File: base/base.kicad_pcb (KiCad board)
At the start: 2 copper layers, 51.2 x 20.5 mm, 12 parts, among them J1 Game Boy, J2 Game Gear, J3 Programming, U1 HC139, U2 PIC10F200-IOT

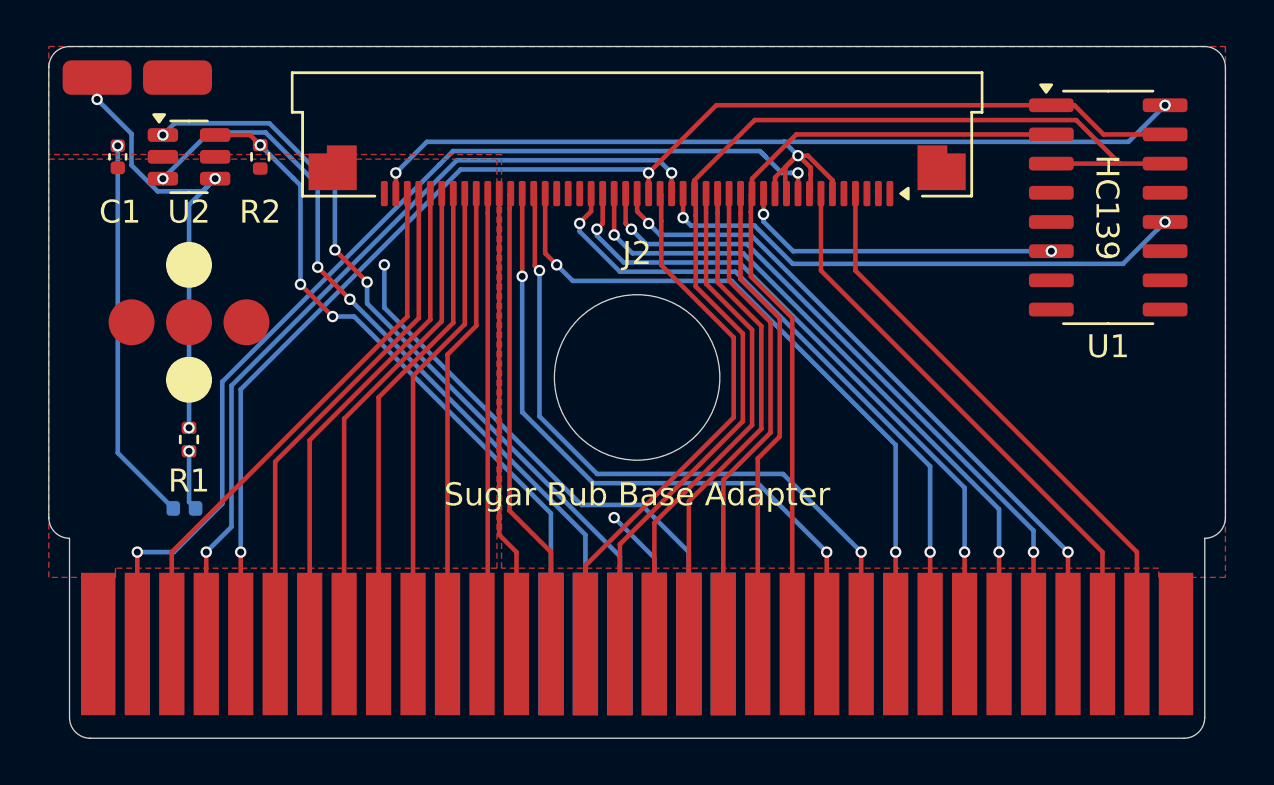
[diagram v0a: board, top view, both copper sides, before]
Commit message: Narrow fingers and move D1 to right side
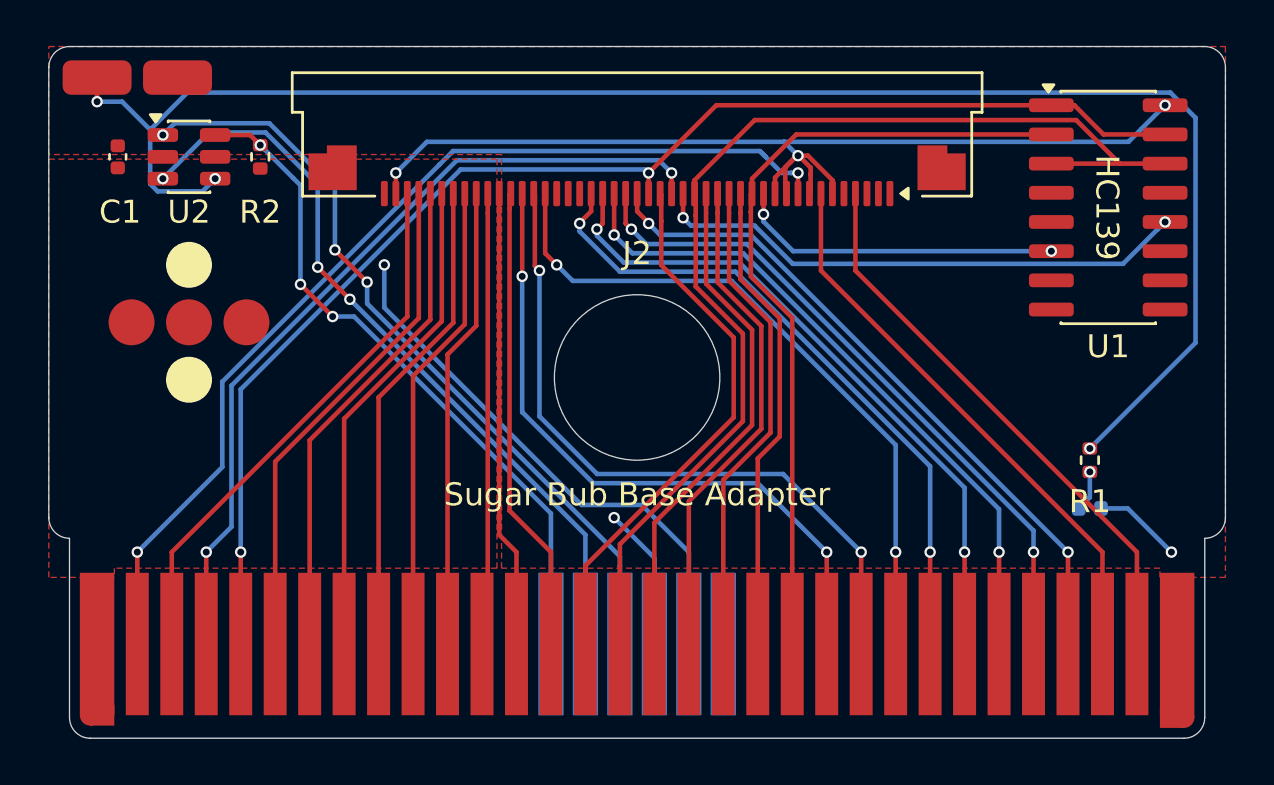
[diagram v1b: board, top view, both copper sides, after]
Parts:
- moved D1 39.4 mm to (119.7, 98.1), turned to 180 degrees
- moved R1 39.2 mm to (119.7, 96.0)
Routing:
- net Net-(U2-GP2): track 19.7 -> 72.3 mm
- net GND: track 23.0 -> 10.1 mm
- net CLK: track 44.7 -> 43.7 mm
- net Net-(D1-A): track 2.61 -> 1.79 mm

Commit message: Adjust adapter PCB dimensions
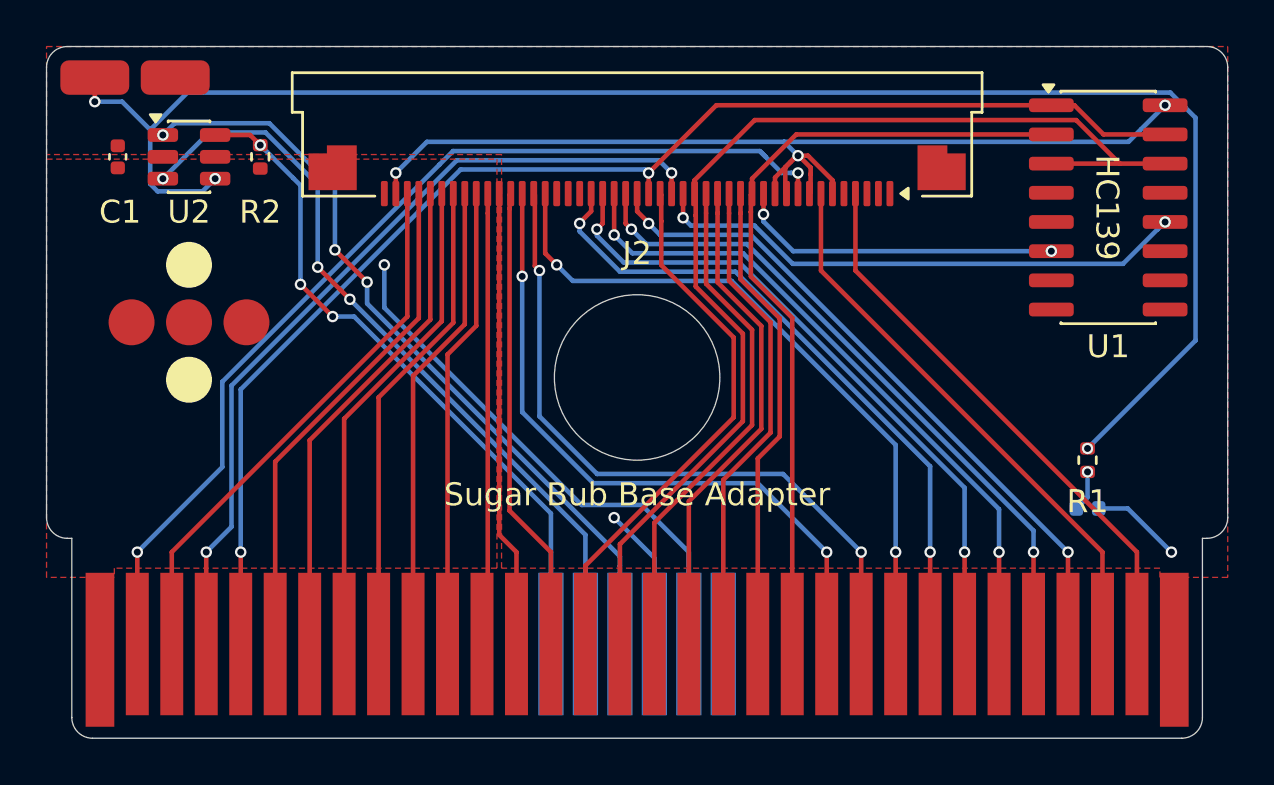
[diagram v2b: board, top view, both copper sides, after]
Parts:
- moved D1 0.10 mm to (119.6, 98.1)
- moved R1 0.10 mm to (119.6, 96.0)
- moved TP1 0.10 mm to (76.4, 79.3)
- moved TP2 0.10 mm to (79.9, 79.3)
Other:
- board size 51.2 x 20.5 mm -> 51.4 x 20.5 mm
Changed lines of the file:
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@@
 	(footprint "Connector_Wire:SolderWirePad_1x01_SMD_1.5x3mm"
 		(layer "F.Cu")
-		(at 80 79.35 90)
+		(at 79.9 79.35 90)
 		(descr "Wire Pad, Square, SMD Pad,  1.5mm x 3mm")
 		(tags "MeasurementPoint Square SMDPad 1.5mmx3mm ")
@@
 	(footprint "Connector_Wire:SolderWirePad_1x01_SMD_1.5x3mm"
 		(layer "F.Cu")
-		(at 76.5 79.35 90)
+		(at 76.4 79.35 90)
 		(descr "Wire Pad, Square, SMD Pad,  1.5mm x 3mm")
 		(tags "MeasurementPoint Square SMDPad 1.5mmx3mm ")
@@
 		(attr smd)
 		(fp_line
-			(start -24.7 3.2)
-			(end -24.7 -4.6)
+			(start -24.6 -4.6)
+			(end -24.8 -4.6)
 			(stroke
 				(width 0.05)
@@
 		)
 		(fp_line
-			(start -23.8 4.1)
-			(end 23.8 4.1)
+			(start -24.6 3.2)
+			(end -24.6 -4.6)
+			(stroke
+				(width 0.05)
+				(type default)
+			)
+			(layer "Edge.Cuts")
+		)
+		(fp_line
+			(start -23.7 4.1)
+			(end 23.7 4.1)
 			(stroke
 				(width 0.05)
@@
 		)
 		(fp_line
-			(start 24.7 3.2)
-			(end 24.7 -4.6)
+			(start 24.6 -4.6)
+			(end 24.8 -4.6)
+			(stroke
+				(width 0.05)
+				(type default)
+			)
+			(layer "Edge.Cuts")
+		)
+		(fp_line
+			(start 24.6 3.2)
+			(end 24.6 -4.6)
 			(stroke
 				(width 0.05)
@@
 		)
 		(fp_arc
-			(start -24.7 -4.6)
-			(mid -25.336396 -4.863604)
-			(end -25.6 -5.5)
+			(start -24.8 -4.6)
+			(mid -25.436396 -4.863604)
+			(end -25.7 -5.5)
 			(stroke
 				(width 0.05)
@@
 		)
 		(fp_arc
-			(start -23.8 4.1)
-			(mid -24.436396 3.836396)
-			(end -24.7 3.2)
+			(start -23.7 4.1)
+			(mid -24.336396 3.836396)
+			(end -24.6 3.2)
 			(stroke
 				(width 0.05)
@@
 		)
 		(fp_arc
-			(start 24.7 3.2)
-			(mid 24.436396 3.836396)
-			(end 23.8 4.1)
+			(start 24.6 3.2)
+			(mid 24.336396 3.836396)
+			(end 23.7 4.1)
 			(stroke
 				(width 0.05)
@@
 		)
 		(fp_arc
-			(start 25.6 -5.5)
-			(mid 25.336396 -4.863604)
-			(end 24.7 -4.6)
+			(start 25.7 -5.5)
+			(mid 25.436396 -4.863604)
+			(end 24.8 -4.6)
 			(stroke
 				(width 0.05)
@@
 			(layer "F.CrtYd")
 		)
-		(pad "1" connect circle
-			(at -23.8 3.1)
-			(size 0.9 0.9)
-			(layers "F.Cu" "F.Mask")
-			(net 26 "+5V")
-			(pinfunction "Pin_1")
-			(pintype "passive")
-		)
-		(pad "1" connect rect
-			(at -23.5 0)
-			(size 1.5 6.2)
-			(layers "F.Cu" "F.Mask")
-			(net 26 "+5V")
-			(pinfunction "Pin_1")
-			(pintype "passive")
-		)
 		(pad "1" connect rect
-			(at -23.275 3.1)
-			(size 1.05 0.9)
+			(at -23.375 0.25)
+			(size 1.25 6.7)
 			(layers "F.Cu" "F.Mask")
 			(net 26 "+5V")
@@
 		)
 		(pad "32" connect rect
-			(at 23.275 3.2)
-			(size 1.05 0.9)
-			(layers "F.Cu" "F.Mask")
-			(net 24 "GND")
-			(pinfunction "Pin_32")
-			(pintype "passive")
-		)
-		(pad "32" connect rect
-			(at 23.5 0.05)
-			(size 1.5 6.3)
-			(layers "F.Cu" "F.Mask")
-			(net 24 "GND")
-			(pinfunction "Pin_32")
-			(pintype "passive")
-		)
-		(pad "32" connect circle
-			(at 23.8 3.2)
-			(size 0.9 0.9)
+			(at 23.375 0.25)
+			(size 1.25 6.7)
 			(layers "F.Cu" "F.Mask")
 			(net 24 "GND")
@@
 	(footprint "Resistor_SMD:R_0402_1005Metric"
 		(layer "F.Cu")
-		(at 119.7 96 -90)
+		(at 119.6 96 -90)
 		(descr "Resistor SMD 0402 (1005 Metric), square (rectangular) end terminal, IPC-7351 nominal, (Body size source: IPC-SM-782 page 72, https://www.pcb-3d.com/wordpress/wp-content/uploads/ipc-sm-782a_amendment_1_and_2.pdf), generated with kicad-footprint-generator")
 		(tags "resistor")
@@
 		)
 		(property "Value" "Game Gear"
-			(at 0 3.45 180)
+			(at 0 4.5 180)
 			(layer "F.Fab")
 			(effects
@@
 			(layer "F.Fab")
 		)
-		(fp_text user "${REFERENCE}"
-			(at 0 0 180)
-			(layer "F.Fab")
-			(effects
-				(font
-					(size 1 1)
-					(thickness 0.15)
-				)
-			)
-		)
 		(pad "1" smd roundrect
 			(at 11 -2.9)
@@
 	(footprint "LED_SMD:LED_0402_1005Metric"
 		(layer "B.Cu")
-		(at 119.7 98.1 180)
+		(at 119.6 98.1 180)
 		(descr "LED SMD 0402 (1005 Metric), square (rectangular) end terminal, IPC-7351 nominal, (Body size source: http://www.tortai-tech.com/upload/download/2011102023233369053.pdf), generated with kicad-footprint-generator")
 		(tags "LED")
@@
 	)
 	(gr_line
-		(start 124.7 78)
-		(end 75.3 78)
+		(start 124.8 78)
+		(end 75.2 78)
 		(stroke
 			(width 0.05)
@@
 	)
 	(gr_line
-		(start 125.6 98.5)
-		(end 125.6 78.9)
+		(start 125.7 98.5)
+		(end 125.7 78.9)
 		(stroke
 			(width 0.05)
@@
 	)
 	(gr_arc
-		(start 124.7 78)
-		(mid 125.336396 78.263604)
-		(end 125.6 78.9)
+		(start 124.8 78)
+		(mid 125.436396 78.263604)
+		(end 125.7 78.9)
 		(stroke
 			(width 0.05)
@@
 	)
 	(gr_arc
-		(start 74.4 78.9)
-		(mid 74.663604 78.263604)
-		(end 75.3 78)
+		(start 74.3 78.9)
+		(mid 74.563604 78.263604)
+		(end 75.2 78)
 		(stroke
 			(width 0.05)
@@
 	)
 	(gr_line
-		(start 74.4 98.5)
-		(end 74.4 78.9)
+		(start 74.3 98.5)
+		(end 74.3 78.9)
 		(stroke
 			(width 0.05)
@@
 		(layer "Dwgs.User")
 		(pts
-			(xy 124.7 107.2) (xy 119.7 98.1)
+			(xy 124.6 107.2) (xy 119.6 98.1)
 		)
 		(height 4.8)
@@
 		)
 		(gr_text "5"
-			(at 122.2 110.85 0)
+			(at 122.1 110.85 0)
 			(layer "Dwgs.User")
 			(effects
@@
 		(layer "Dwgs.User")
 		(pts
-			(xy 74.4 98.5) (xy 125.6 98.5)
+			(xy 74.3 98.5) (xy 125.7 98.5)
 		)
 		(height 18.5)
@@
 			(keep_text_aligned yes)
 		)
-		(gr_text "51.2"
+		(gr_text "51.4"
 			(at 100 115.85 0)
 			(layer "Dwgs.User")
@@
 		(layer "Dwgs.User")
 		(pts
-			(xy 75.3 107.2) (xy 124.7 107.2)
+			(xy 75.4 107.2) (xy 124.6 107.2)
 		)
 		(height 7.3)
@@
 			(keep_text_aligned yes)
 		)
-		(gr_text "49.4"
+		(gr_text "49.2"
 			(at 100 113.35 0)
 			(layer "Dwgs.User")
@@
 			(xy 123.8 108.1) (xy 119.7 98.1)
 		)
-		(height 4.2)
+		(height 5.2)
 		(orientation 1)
 		(format
@@
 		)
 		(gr_text "10"
-			(at 126.85 103.1 90)
+			(at 127.85 103.1 90)
 			(layer "Dwgs.User")
 			(effects
@@
 	)
 	(segment
-		(start 120.185 98.1)
-		(end 121.35 98.1)
+		(start 100.75 104)
+		(end 100.75 100.25)
 		(width 0.2)
 		(layer "B.Cu")
@@
 	)
 	(segment
-		(start 100.75 104)
-		(end 100.75 100.25)
+		(start 120.085 98.1)
+		(end 121.35 98.1)
 		(width 0.2)
 		(layer "B.Cu")
@@
 	)
 	(via
-		(at 119.7 96.51)
+		(at 119.6 96.51)
 		(size 0.5)
 		(drill 0.3)
@@
 	)
 	(segment
-		(start 119.215 98.1)
-		(end 119.7 97.615)
+		(start 119.115 98.1)
+		(end 119.6 97.615)
 		(width 0.2)
 		(layer "B.Cu")
@@
 	)
 	(segment
-		(start 119.7 96.51)
-		(end 119.7 97.615)
+		(start 119.6 96.51)
+		(end 119.6 97.615)
 		(width 0.2)
 		(layer "B.Cu")
@@
 	)
 	(segment
-		(start 76.5 80.4)
-		(end 76.5 79.35)
+		(start 76.4 80.4)
+		(end 76.4 79.35)
 		(width 0.2)
 		(layer "F.Cu")
@@
 	)
 	(via
-		(at 76.5 80.4)
+		(at 76.4 80.4)
 		(size 0.5)
 		(drill 0.3)
@@
 	)
 	(via
-		(at 119.7 95.49)
+		(at 119.6 95.49)
 		(size 0.5)
 		(drill 0.3)
@@
 	)
 	(segment
-		(start 77.589732 80.4)
-		(end 76.5 80.4)
+		(start 119.6 95.49)
+		(end 124.3 90.79)
 		(width 0.2)
 		(layer "B.Cu")
@@
 	)
 	(segment
-		(start 124.3 90.89)
+		(start 124.3 90.79)
 		(end 124.3 81.100768)
 		(width 0.2)
@@
 	)
 	(segment
-		(start 119.7 95.49)
-		(end 124.3 90.89)
-		(width 0.2)
-		(layer "B.Cu")
-		(net 50)
-	)
-	(segment
 		(start 81.6375 83.75)
 		(end 81.0865 84.301)
@@
 		(net 50)
 	)
+	(segment
+		(start 76.4 80.4)
+		(end 77.589732 80.4)
+		(width 0.2)
+		(layer "B.Cu")
+		(net 50)
+	)
 	(zone
 		(net 26)
@@
 		(polygon
 			(pts
-				(xy 74.4 82.9) (xy 93.9 82.9) (xy 93.9 100.700606) (xy 77.25 100.7) (xy 77.25 101.1) (xy 74.4 101.1)
+				(xy 74.3 82.9) (xy 93.9 82.9) (xy 93.9 100.700606) (xy 77.25 100.7) (xy 77.25 101.1) (xy 74.3 101.1)
 			)
 		)
@@
 		(polygon
 			(pts
-				(xy 94.1 82.7) (xy 74.4 82.7) (xy 74.4 78) (xy 125.6 78) (xy 125.6 101.1) (xy 122.75 101.1) (xy 122.75 100.7)
+				(xy 94.1 82.7) (xy 74.3 82.7) (xy 74.3 78) (xy 125.7 78) (xy 125.7 101.1) (xy 122.75 101.1) (xy 122.75 100.7)
 				(xy 94.1 100.7)
 			)

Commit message: Make cap and resistors 0805 for easier soldering
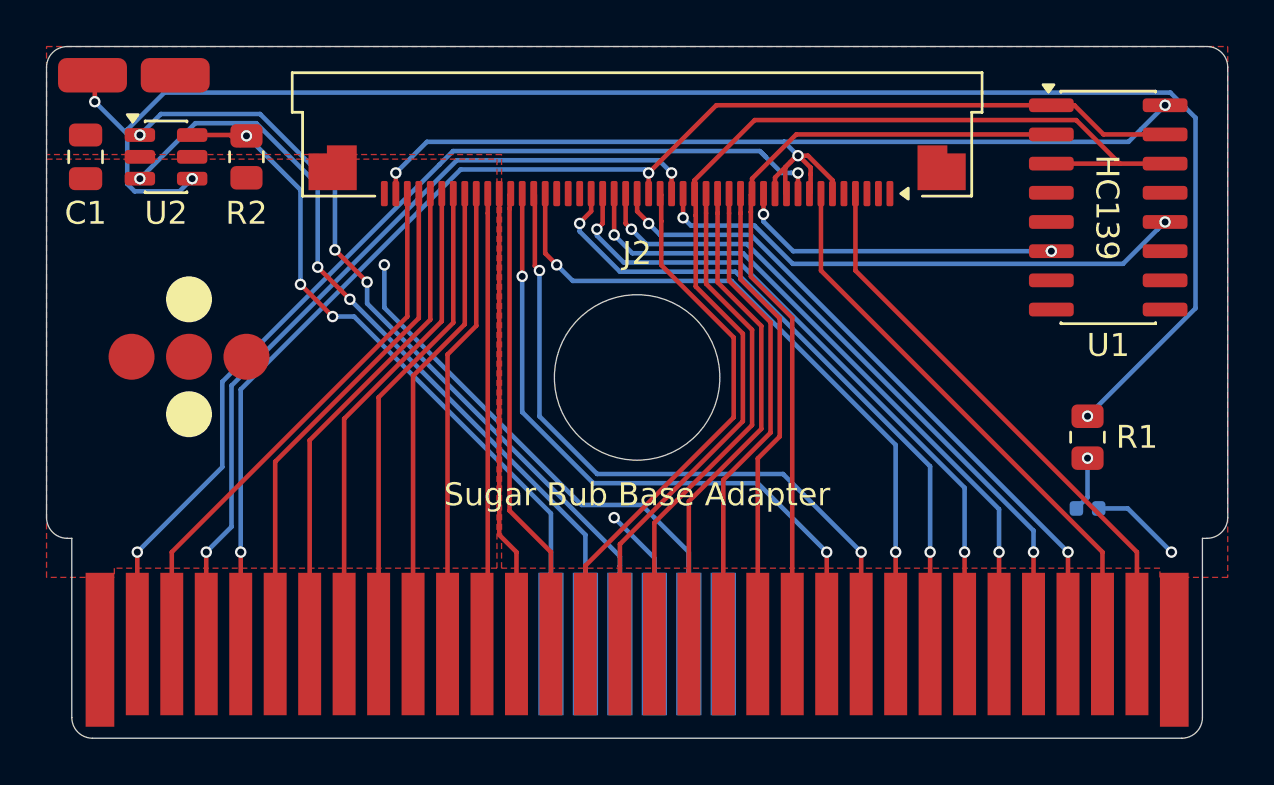
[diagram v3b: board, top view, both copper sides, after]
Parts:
- C1: footprint Capacitor_SMD:C_0402_1005Metric -> Capacitor_SMD:C_0805_2012Metric
- R1, R2: footprint Resistor_SMD:R_0402_1005Metric -> Resistor_SMD:R_0805_2012Metric
- moved TP3 1.50 mm to (80.5, 91.5)
- moved C1 1.40 mm to (76.0, 82.8)
- moved R1 1.00 mm to (119.6, 95.0)
- moved U2 1.00 mm to (79.5, 82.8)
- moved R2 0.60 mm to (83.0, 82.8)
- moved TP1 0.14 mm to (76.3, 79.2)
- moved TP2 0.10 mm to (79.9, 79.2)
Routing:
- net Net-(J3-Pin_5): track 33.3 -> 34.7 mm
- net Net-(J3-Pin_4): track 33.8 -> 35.2 mm
- net Net-(U2-GP2): track 72.5 -> 71.1 mm
- net Net-(J3-Pin_6): track 29.6 -> 30.3 mm
- net Net-(D1-A): track 1.79 -> 2.39 mm
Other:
- board text added: "Finish: ENIG Thickness: 0.8mm"
